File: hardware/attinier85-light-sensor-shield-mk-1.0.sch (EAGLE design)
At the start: 6 parts, among them U1 ATTINIEST85_SHIELDV2

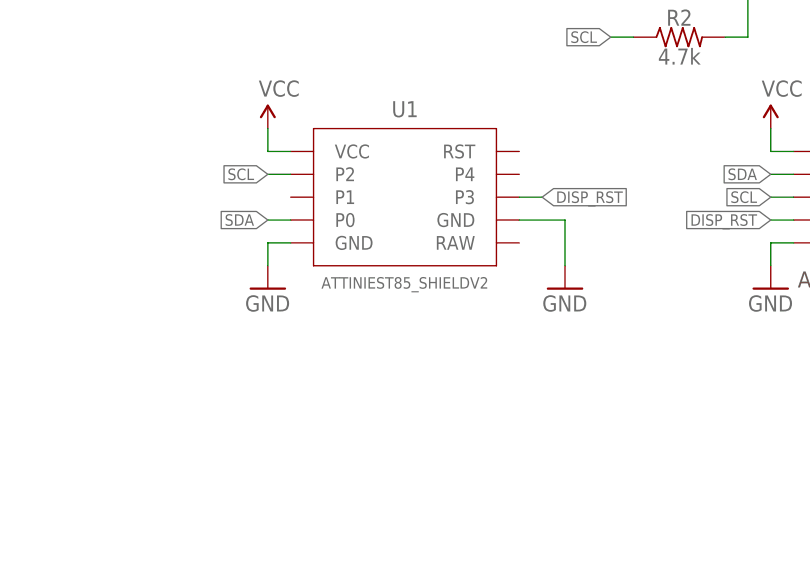
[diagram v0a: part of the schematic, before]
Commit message: renaming parts
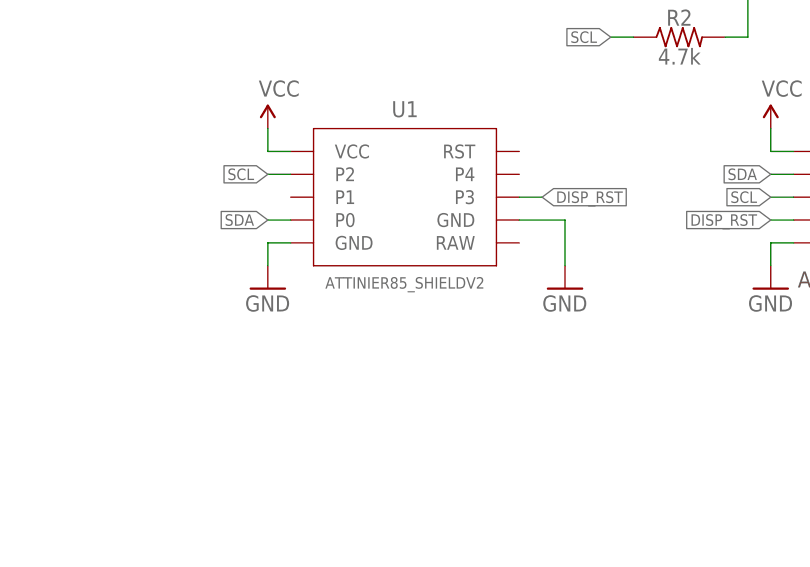
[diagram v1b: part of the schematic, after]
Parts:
- U1: value ATTINIEST85_SHIELDV2 -> ATTINIER85_SHIELDV2; device A_butts:ATTINIEST85_SHIELDV2 -> A_butts:ATTINIER85_SHIELDV2
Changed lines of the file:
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@@
 <grid distance="100" unitdist="mil" unit="mil" style="lines" multiple="1" display="yes" altdistance="2" altunitdist="mil" altunit="mil"/>
 <layers>
-<layer number="1" name="Top" color="4" fill="1" visible="yes" active="no"/>
-<layer number="16" name="Bottom" color="1" fill="1" visible="yes" active="no"/>
-<layer number="17" name="Pads" color="2" fill="1" visible="yes" active="no"/>
-<layer number="18" name="Vias" color="2" fill="1" visible="yes" active="no"/>
-<layer number="19" name="Unrouted" color="6" fill="1" visible="yes" active="no"/>
-<layer number="20" name="Dimension" color="15" fill="1" visible="yes" active="no"/>
-<layer number="21" name="tPlace" color="7" fill="1" visible="yes" active="no"/>
-<layer number="22" name="bPlace" color="7" fill="1" visible="yes" active="no"/>
-<layer number="23" name="tOrigins" color="15" fill="1" visible="yes" active="no"/>
-<layer number="24" name="bOrigins" color="15" fill="1" visible="yes" active="no"/>
-<layer number="25" name="tNames" color="7" fill="1" visible="yes" active="no"/>
-<layer number="26" name="bNames" color="7" fill="1" visible="yes" active="no"/>
-<layer number="27" name="tValues" color="7" fill="1" visible="yes" active="no"/>
-<layer number="28" name="bValues" color="7" fill="1" visible="yes" active="no"/>
+<layer number="1" name="Top" color="4" fill="1" visible="no" active="no"/>
+<layer number="16" name="Bottom" color="1" fill="1" visible="no" active="no"/>
+<layer number="17" name="Pads" color="2" fill="1" visible="no" active="no"/>
+<layer number="18" name="Vias" color="2" fill="1" visible="no" active="no"/>
+<layer number="19" name="Unrouted" color="6" fill="1" visible="no" active="no"/>
+<layer number="20" name="Dimension" color="15" fill="1" visible="no" active="no"/>
+<layer number="21" name="tPlace" color="7" fill="1" visible="no" active="no"/>
+<layer number="22" name="bPlace" color="7" fill="1" visible="no" active="no"/>
+<layer number="23" name="tOrigins" color="15" fill="1" visible="no" active="no"/>
+<layer number="24" name="bOrigins" color="15" fill="1" visible="no" active="no"/>
+<layer number="25" name="tNames" color="7" fill="1" visible="no" active="no"/>
+<layer number="26" name="bNames" color="7" fill="1" visible="no" active="no"/>
+<layer number="27" name="tValues" color="7" fill="1" visible="no" active="no"/>
+<layer number="28" name="bValues" color="7" fill="1" visible="no" active="no"/>
 <layer number="29" name="tStop" color="7" fill="3" visible="no" active="no"/>
 <layer number="30" name="bStop" color="7" fill="6" visible="no" active="no"/>
@@
 <layer number="35" name="tGlue" color="7" fill="4" visible="no" active="no"/>
 <layer number="36" name="bGlue" color="7" fill="5" visible="no" active="no"/>
-<layer number="37" name="tTest" color="7" fill="1" visible="yes" active="no"/>
-<layer number="38" name="bTest" color="7" fill="1" visible="yes" active="no"/>
+<layer number="37" name="tTest" color="7" fill="1" visible="no" active="no"/>
+<layer number="38" name="bTest" color="7" fill="1" visible="no" active="no"/>
 <layer number="39" name="tKeepout" color="4" fill="11" visible="no" active="no"/>
 <layer number="40" name="bKeepout" color="1" fill="11" visible="no" active="no"/>
@@
 <layer number="44" name="Drills" color="7" fill="1" visible="no" active="no"/>
 <layer number="45" name="Holes" color="7" fill="1" visible="no" active="no"/>
-<layer number="46" name="Milling" color="3" fill="1" visible="yes" active="no"/>
-<layer number="47" name="Measures" color="7" fill="1" visible="yes" active="no"/>
-<layer number="48" name="Document" color="7" fill="1" visible="yes" active="no"/>
-<layer number="49" name="Reference" color="7" fill="1" visible="yes" active="no"/>
-<layer number="50" name="dxf" color="7" fill="1" visible="yes" active="no"/>
-<layer number="51" name="tDocu" color="7" fill="1" visible="yes" active="no"/>
-<layer number="52" name="bDocu" color="7" fill="1" visible="yes" active="no"/>
-<layer number="53" name="tGND_GNDA" color="7" fill="9" visible="yes" active="no"/>
-<layer number="54" name="bGND_GNDA" color="1" fill="9" visible="yes" active="no"/>
-<layer number="56" name="wert" color="7" fill="1" visible="yes" active="no"/>
-<layer number="57" name="tCAD" color="7" fill="1" visible="yes" active="no"/>
+<layer number="46" name="Milling" color="3" fill="1" visible="no" active="no"/>
+<layer number="47" name="Measures" color="7" fill="1" visible="no" active="no"/>
+<layer number="48" name="Document" color="7" fill="1" visible="no" active="no"/>
+<layer number="49" name="Reference" color="7" fill="1" visible="no" active="no"/>
+<layer number="50" name="dxf" color="7" fill="1" visible="no" active="no"/>
+<layer number="51" name="tDocu" color="7" fill="1" visible="no" active="no"/>
+<layer number="52" name="bDocu" color="7" fill="1" visible="no" active="no"/>
+<layer number="53" name="tGND_GNDA" color="7" fill="9" visible="no" active="no"/>
+<layer number="54" name="bGND_GNDA" color="1" fill="9" visible="no" active="no"/>
+<layer number="56" name="wert" color="7" fill="1" visible="no" active="no"/>
+<layer number="57" name="tCAD" color="7" fill="1" visible="no" active="no"/>
 <layer number="90" name="Modules" color="5" fill="1" visible="yes" active="yes"/>
 <layer number="91" name="Nets" color="2" fill="1" visible="yes" active="yes"/>
@@
 <parts>
 <part name="FRAME1" library="A_butts" deviceset="FRAME-LETTER" device="NO_PACKAGE"/>
-<part name="U1" library="A_butts" deviceset="ATTINIEST85_SHIELD" device="V2"/>
+<part name="U1" library="A_butts" deviceset="ATTINIER85_SHIELD" device="V2"/>
 <part name="SUPPLY1" library="A_butts" deviceset="VCC" device=""/>
 <part name="GND1" library="A_butts" deviceset="GND" device=""/>
